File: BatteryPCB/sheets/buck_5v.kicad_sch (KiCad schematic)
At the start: 9 parts, among them U1 LMR51430XFDDCR

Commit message: Battery PCB v17: test points, strict design rules, review fixes
- Test points: TP1 +5V (buck output), TP2 VBAT+ (2S pack), TP3/TP4 GND;
  2 mm through-hole pads placed where both sides are open
- Strict rules in the project: 0.25/0.3/0.4 mm clearance (signal/power/pyro),
  0.3 mm hole clearance, 0.5 mm hole-to-hole, 0.15 mm via ring, silk spacing;
  every DRC check is an error. Fixed the spots they flagged around U1, R4, C8,
  D1/D3 silk and the TP4 label
- R5 47k -> 39k so VBAT_SENSE stays inside the ESP32 ADC range at a full pack
- BOM note: the RunCam needs a built harness (3-pin power/video + RX/TX pads)
- README: exact ESP32 to buy (ESP32-DevKitC-32E, not WROVER or 30-pin clones),
  design rules, sense scaling; layout notes for v17
- Checks: ERC 0 errors; DRC 0 violations incl. warnings with schematic parity;
  all 115 schematic pins match board pad nets; verify_A ALL PASS

Co-Authored-By: Claude Opus 5.5 <noreply@anthropic.com>
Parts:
- added TP1: TP_5V, TestPoint:TestPoint_THTPad_D2.0mm_Drill1.0mm, symbol Connector:TestPoint
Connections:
- net +5V: now also TP1.1
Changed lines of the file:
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@@
 		(effects (font (size 1.8 1.8) (bold yes)) (justify left bottom))
 	)
+	(symbol
+		(lib_id "Connector:TestPoint")
+		(at 127.00 25.40 0)
+		(unit 1)
+		(exclude_from_sim no)
+		(in_bom no)
+		(on_board yes)
+		(dnp no)
+		(property "Reference" "TP1"
+			(at 129.54 20.32 0)
+			(effects (font (size 1.27 1.27)) (justify left))
+		)
+		(property "Value" "TP_5V"
+			(at 129.54 22.86 0)
+			(effects (font (size 1.27 1.27)) (justify left))
+		)
+		(property "Footprint" "TestPoint:TestPoint_THTPad_D2.0mm_Drill1.0mm"
+			(at 127.00 25.40 0)
+			(effects (font (size 1.27 1.27)) (hide yes))
+		)
+		(property "Datasheet" "~"
+			(at 127.00 25.40 0)
+			(effects (font (size 1.27 1.27)) (hide yes))
+		)
+		(property "Description" "Bench test point"
+			(at 127.00 25.40 0)
+			(effects (font (size 1.27 1.27)) (hide yes))
+		)
+		(pin "1")
+		(instances
+			(project "battery_pcb"
+				(path "/19ef3a32-de7c-46ee-a850-2420f6d47f94/1914f4ed-278a-4026-a86a-769e5e361ab6"
+					(reference "TP1")
+					(unit 1)
+				)
+			)
+		)
+	)
+	(wire
+		(pts (xy 127.00 25.40) (xy 127.00 30.48))
+		(stroke (width 0) (type default))
+	)
+	(label "+5V"
+		(at 127.00 30.48 0)
+		(fields_autoplaced yes)
+		(effects (font (size 1.27 1.27)) (justify left bottom))
+	)
 )

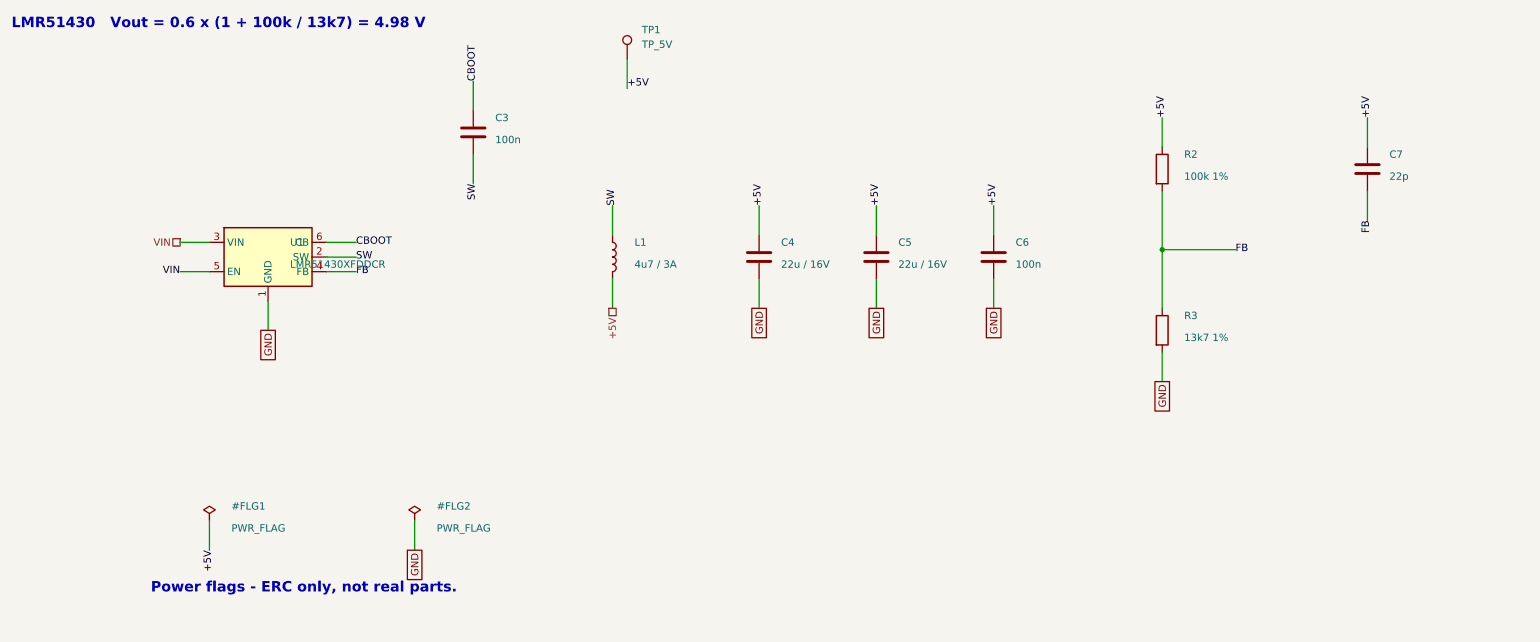
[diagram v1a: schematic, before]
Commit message: Battery PCB v19: UVLO on the buck, input caps, 6.8 uH, wired schematic
Third review (design check of the power path):
- U1 EN gets an R9/R10 divider (UVLO: on 6.3 V, off 5.5 V at VIN) so
  the 2S pack is no longer run down to 1.8 V per cell.
- Input caps per the LMR51430 datasheet: C1 is the 100 nF at U1's pins,
  C2 + new C11 (10 uF) are the bulk.
- L1 6.8 uH (TI's value for 500 kHz / 5 V out), same footprint.
- Sheets 1-3 redrawn with wires; C1/C2 moved next to U1; stale 47k
  divider note and the SS34 value on D3 corrected.
ERC 0 errors, DRC 0 (strict, schematic parity), verify_A all pass.

Co-Authored-By: Claude Opus 5.5 <noreply@anthropic.com>
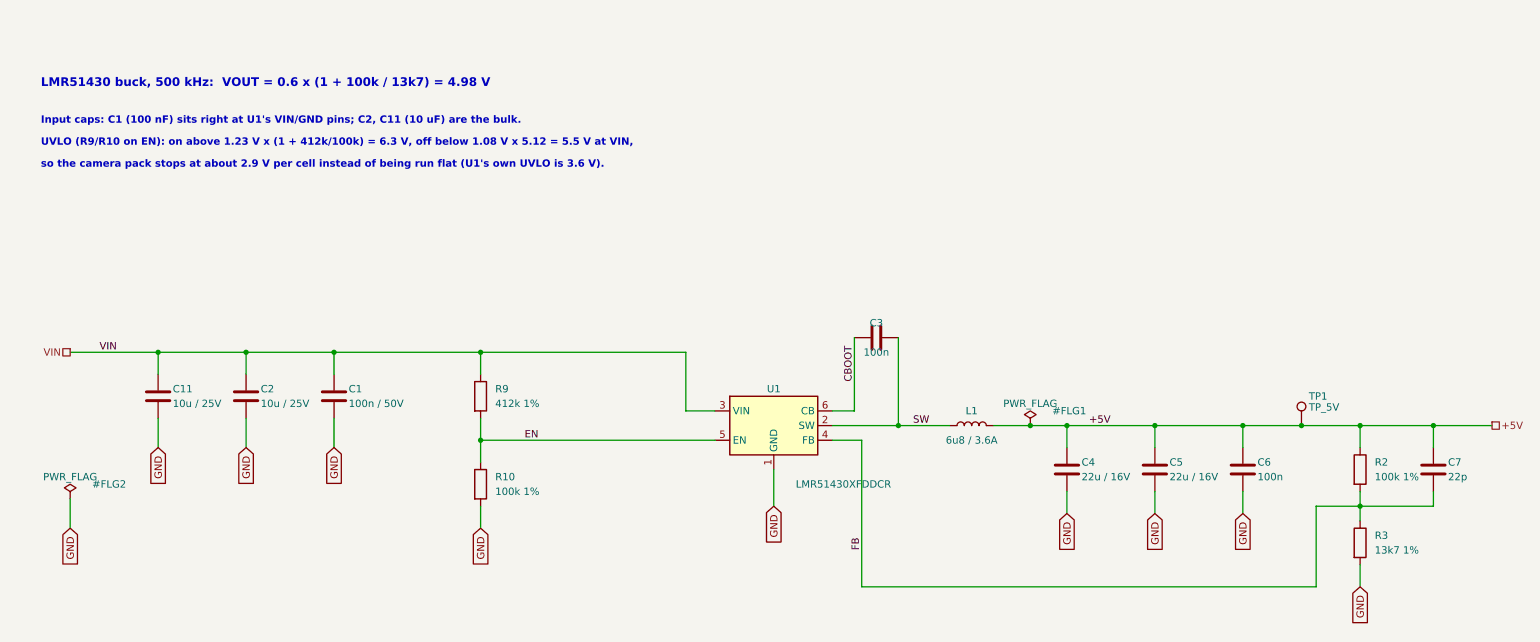
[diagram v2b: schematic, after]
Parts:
- added C1: 100n / 50V, Capacitor_SMD:C_0805_2012Metric, symbol Device:C
- added C11, C2: 10u / 25V, Capacitor_SMD:C_0805_2012Metric, symbol Device:C
- added R10: 100k 1%, Resistor_SMD:R_0603_1608Metric, symbol Device:R
- added R9: 412k 1%, Resistor_SMD:R_0603_1608Metric, symbol Device:R
- L1: value 4u7 / 3A -> 6u8 / 3.6A; MPN SRN6045TA-4R7M -> SRN6045TA-6R8M
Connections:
- net GND: now also C1.2, C11.2, C2.2, R10.2
- net VIN: now also C1.1, C11.1, C2.1, R9.1; no longer U1.5 (EN)
- new net EN: R10.1, R9.2, U1.5 (EN)
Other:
- note added: "Input caps: C1 (100 nF) sits right at U1's VIN/GND pins; C2, C11 (10 uF) are the bulk."
- note added: "LMR51430 buck, 500 kHz: VOUT = 0.6 x (1 + 100k / 13k7) = 4.98 V"
- note added: "UVLO (R9/R10 on EN): on above 1.23 V x (1 + 412k/100k) = 6.3 V, off below 1.08 V x 5.12 = 5.5 V at VIN,"
- note added: "so the camera pack stops at about 2.9 V per cell instead of being run flat (U1's own UVLO is 3.6 V)."
- note removed: "LMR51430 Vout = 0.6 x (1 + 100k / 13k7) = 4.98 V"
- note removed: "Power flags - ERC only, not real parts."
- moved on the sheet: C3, C4, C5, C6, C7, L1, R2, R3, TP1, U1

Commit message: Battery PCB v19.1: LCSC part numbers, R9 402k (412k out of stock)
- BOM: checked LCSC numbers for every soldered part LCSC sells, DigiKey/
  Mouser numbers for the rest (Keystone 1042, Wurth 9774050243R, ESP32).
  J1/J2 LCSC alternative HCTL PM254-1-19-Z-8.5 (Sullins out of stock).
- JLCPCB assembly BOM + CPL (optional).
- R9 412k -> 402k (412k has no LCSC stock): UVLO on 6.2 V, off 5.4 V.
ERC 0 errors, DRC 0 (strict, schematic parity), verify_A all pass.

Co-Authored-By: Claude Opus 5.5 <noreply@anthropic.com>
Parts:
- R9: value 412k 1% -> 402k 1%; MPN RC0603FR-07412KL -> RC0603FR-07402KL
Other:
- note added: "UVLO (R9/R10 on EN): on above 1.23 V x (1 + 402k/100k) = 6.2 V, off below 1.08 V x 5.02 = 5.4 V at VIN,"
- note added: "so the camera pack stops at about 2.85 V per cell instead of being run flat (U1's own UVLO is 3.6 V)."
- note removed: "UVLO (R9/R10 on EN): on above 1.23 V x (1 + 412k/100k) = 6.3 V, off below 1.08 V x 5.12 = 5.5 V at VIN,"
- note removed: "so the camera pack stops at about 2.9 V per cell instead of being run flat (U1's own UVLO is 3.6 V)."
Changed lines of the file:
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@@
 		(effects (font (size 1.27 1.27) (thickness 0.254) (bold yes) (color 0 0 194 1)) (justify left bottom))
 	)
-	(text "UVLO (R9/R10 on EN): on above 1.23 V x (1 + 412k/100k) = 6.3 V, off below 1.08 V x 5.12 = 5.5 V at VIN,"
+	(text "UVLO (R9/R10 on EN): on above 1.23 V x (1 + 402k/100k) = 6.2 V, off below 1.08 V x 5.02 = 5.4 V at VIN,"
 		(exclude_from_sim no)
 		(at 25.40 40.64 0)
 		(effects (font (size 1.27 1.27) (thickness 0.254) (bold yes) (color 0 0 194 1)) (justify left bottom))
 	)
-	(text "so the camera pack stops at about 2.9 V per cell instead of being run flat (U1's own UVLO is 3.6 V)."
+	(text "so the camera pack stops at about 2.85 V per cell instead of being run flat (U1's own UVLO is 3.6 V)."
 		(exclude_from_sim no)
 		(at 25.40 44.45 0)
@@
 			(effects (font (size 1.27 1.27)) (justify left) )
 		)
-		(property "Value" "412k 1%"
+		(property "Value" "402k 1%"
 			(at 104.14 85.09 0)
 			(effects (font (size 1.27 1.27)) (justify left) )
@@
 			(effects (font (size 1.27 1.27)) (hide yes))
 		)
-		(property "MPN" "RC0603FR-07412KL"
-			(at 101.60 83.82 0)
-			(effects (font (size 1.27 1.27)) (hide yes))
+		(property "MPN" "RC0603FR-07402KL"
+			(at 101.60 83.82 0)
+			(effects (font (size 1.27 1.27)) (hide yes))
